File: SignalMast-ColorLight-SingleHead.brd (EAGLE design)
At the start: 13 x 39.8 mm, 4 parts

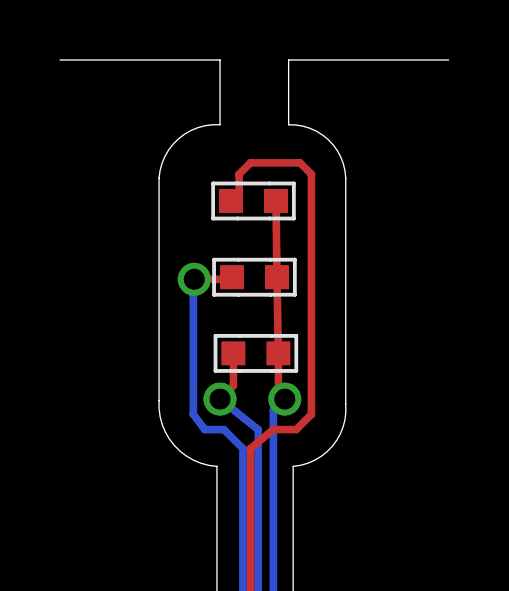
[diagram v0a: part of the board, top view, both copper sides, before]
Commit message: normalized values
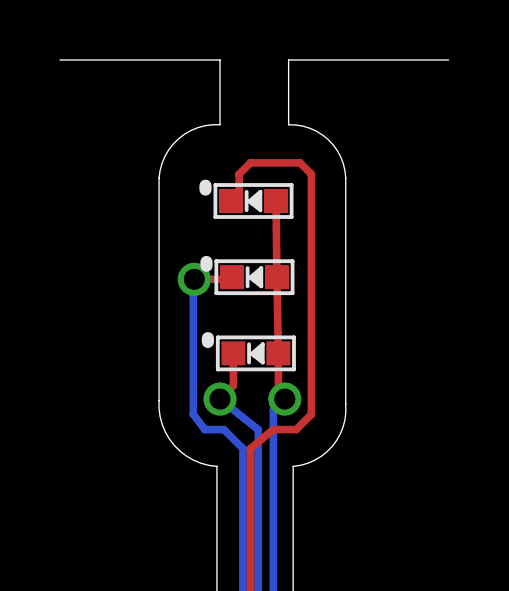
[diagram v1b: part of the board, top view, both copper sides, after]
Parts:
- GYR+: value CONNECTOR-GROVE-4P-2.0-3470130P1 -> 0.100
- turned LED1 to 0 degrees
- turned LED2 to 0 degrees
- turned LED3 to 0 degrees
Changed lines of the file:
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@@
 </autorouter>
 <elements>
-<element name="GYR+" library="SPCoast" package="1X04_LOCK" value="CONNECTOR-GROVE-4P-2.0-3470130P1" x="10.16" y="5.08" smashed="yes" rot="R180">
+<element name="GYR+" library="SPCoast" package="1X04_LOCK" value="0.100" x="10.16" y="5.08" smashed="yes" rot="R180">
 <attribute name="NAME" x="2.921" y="0.762" size="1.778" layer="25" font="vector" ratio="11" rot="SR0"/>
 </element>
-<element name="LED1" library="SPCoast" package="0603-LED" value="R" x="6.53" y="38.099" smashed="yes" rot="R180">
-<attribute name="OPL" value="19-217-R6C-AL1M2VY-3T" x="6.53" y="38.099" size="1.778" layer="27" rot="R180" display="off"/>
-<attribute name="VALUE" x="11.61" y="38.734" size="1.27" layer="27" rot="R180"/>
+<element name="LED1" library="SPCoast" package="0603-LED" value="R" x="6.53" y="38.099" smashed="yes">
+<attribute name="OPL" value="19-217-R6C-AL1M2VY-3T" x="6.53" y="38.099" size="1.778" layer="27" display="off"/>
+<attribute name="VALUE" x="1.45" y="37.464" size="1.27" layer="27"/>
 </element>
-<element name="LED2" library="SPCoast" package="0603-LED" value="Y" x="6.482" y="40.639" smashed="yes" rot="R180">
-<attribute name="OPL" value="19-217-Y5C-AM1N1VY-3T" x="6.482" y="40.639" size="1.778" layer="27" rot="R180" display="off"/>
-<attribute name="VALUE" x="11.562" y="41.274" size="1.27" layer="27" rot="R180"/>
+<element name="LED2" library="SPCoast" package="0603-LED" value="Y" x="6.482" y="40.639" smashed="yes">
+<attribute name="OPL" value="19-217-Y5C-AM1N1VY-3T" x="6.482" y="40.639" size="1.778" layer="27" display="off"/>
+<attribute name="VALUE" x="1.402" y="40.004" size="1.27" layer="27"/>
 </element>
-<element name="LED3" library="SPCoast" package="0603-LED" value="G" x="6.45" y="43.179" smashed="yes" rot="R180">
-<attribute name="OPL" value="19-217-G7C-AN1P2-3T " x="6.45" y="43.179" size="1.778" layer="27" rot="R180" display="off"/>
-<attribute name="VALUE" x="11.53" y="43.814" size="1.27" layer="27" rot="R180"/>
+<element name="LED3" library="SPCoast" package="0603-LED" value="G" x="6.45" y="43.179" smashed="yes">
+<attribute name="OPL" value="19-217-G7C-AN1P2-3T " x="6.45" y="43.179" size="1.778" layer="27" display="off"/>
+<attribute name="VALUE" x="1.37" y="42.544" size="1.27" layer="27"/>
 </element>
 </elements>

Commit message: Version 1.3
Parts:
- renumbered GYR+ to J
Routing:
- net BY: track 38.7 -> 37.7 mm
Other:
- board size 13 x 39.8 mm -> 12.8 x 48.3 mm
- board text added: "+"
- board text added: "G"
- board text added: "R"
- board text added: "Y"
- board text removed: "GYR+"
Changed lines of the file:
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@@
 <setting verticaltext="up"/>
 </settings>
-<grid distance="50" unitdist="mil" unit="mil" style="dots" multiple="2" display="yes" altdistance="25" altunitdist="mil" altunit="mil"/>
+<grid distance="50" unitdist="mil" unit="mil" style="dots" multiple="2" display="yes" altdistance="5" altunitdist="mil" altunit="mil"/>
 <layers>
 <layer number="1" name="Top" color="4" fill="1" visible="yes" active="yes"/>
@@
 <layer number="19" name="Unrouted" color="6" fill="1" visible="yes" active="yes"/>
 <layer number="20" name="Dimension" color="15" fill="1" visible="yes" active="yes"/>
-<layer number="21" name="tPlace" color="19" fill="1" visible="yes" active="yes"/>
+<layer number="21" name="tPlace" color="7" fill="1" visible="yes" active="yes"/>
 <layer number="22" name="bPlace" color="17" fill="1" visible="no" active="yes"/>
 <layer number="23" name="tOrigins" color="30" fill="1" visible="yes" active="yes"/>
@@
 <wire x1="7.7724" y1="34.332" x2="7.7724" y2="8.128" width="0" layer="20"/>
 <wire x1="0" y1="8.128" x2="5.2324" y2="8.128" width="0" layer="20"/>
-<text x="2.921" y="0.762" size="1.778" layer="1" font="vector" rot="SR0">GYR+</text>
+<text x="1.651" y="0.762" size="1.778" layer="21" font="vector" rot="SR0">G</text>
 <wire x1="3.302" y1="43.942" x2="5.334" y2="45.72" width="0" layer="20" curve="-90"/>
 <wire x1="9.525" y1="43.942" x2="7.62" y2="45.72" width="0" layer="20" curve="90"/>
-<rectangle x1="0" y1="-0.127" x2="12.827" y2="47.752" layer="52"/>
-<rectangle x1="-0.127" y1="0" x2="12.7" y2="34.29" layer="51"/>
-<wire x1="7.62" y1="47.879" x2="7.62" y2="45.72" width="0" layer="20"/>
-<wire x1="5.334" y1="45.72" x2="5.334" y2="47.879" width="0" layer="20"/>
-<wire x1="7.7724" y1="8.128" x2="12.8524" y2="8.128" width="0" layer="20"/>
-<wire x1="0" y1="47.879" x2="5.334" y2="47.879" width="0" layer="20"/>
-<wire x1="7.62" y1="47.879" x2="12.954" y2="47.879" width="0" layer="20"/>
-<rectangle x1="5.334" y1="45.72" x2="7.62" y2="47.879" layer="51"/>
+<rectangle x1="0" y1="-0.127" x2="12.827" y2="47.752" layer="22"/>
+<wire x1="7.62" y1="48.26" x2="7.62" y2="45.72" width="0" layer="20"/>
+<wire x1="5.334" y1="45.72" x2="5.334" y2="48.26" width="0" layer="20"/>
+<wire x1="7.7724" y1="8.128" x2="12.827" y2="8.128" width="0" layer="20"/>
+<wire x1="0" y1="48.26" x2="5.334" y2="48.26" width="0" layer="20"/>
+<wire x1="7.62" y1="48.26" x2="12.827" y2="48.26" width="0" layer="20"/>
+<rectangle x1="5.334" y1="45.72" x2="7.62" y2="48.26" layer="21"/>
+<text x="4.191" y="0.762" size="1.778" layer="21" font="vector" rot="SR0">Y</text>
+<text x="6.731" y="0.762" size="1.778" layer="21" font="vector" rot="SR0">R</text>
+<text x="9.271" y="0.762" size="2.1844" layer="21" font="vector" rot="SR0">+</text>
+<rectangle x1="5.2324" y1="8.128" x2="7.7724" y2="34.3408" layer="21"/>
+<rectangle x1="0" y1="3.556" x2="12.827" y2="8.128" layer="21"/>
+<wire x1="0" y1="48.26" x2="0" y2="0" width="0" layer="20"/>
+<wire x1="0" y1="0" x2="12.827" y2="0" width="0" layer="20"/>
+<wire x1="12.827" y1="0" x2="12.827" y2="8.128" width="0" layer="20"/>
+<wire x1="12.827" y1="8.128" x2="12.827" y2="48.26" width="0" layer="20"/>
 </plain>
 <attributes>
@@
 </autorouter>
 <elements>
-<element name="GYR+" library="SPCoast" package="1X04_LOCK" value="0.100" x="10.16" y="5.08" smashed="yes" rot="R180">
-<attribute name="NAME" x="2.921" y="0.762" size="1.778" layer="25" font="vector" ratio="11" rot="SR0"/>
+<element name="J" library="SPCoast" package="1X04_LOCK" value="0.100" x="10.16" y="5.08" smashed="yes" rot="R180">
+<attribute name="NAME" x="1.651" y="9.652" size="1.778" layer="25" font="vector" ratio="11" rot="SR0"/>
 </element>
 <element name="LED1" library="SPCoast" package="0603-LED" value="R" x="6.53" y="38.099" smashed="yes">
 <attribute name="OPL" value="19-217-R6C-AL1M2VY-3T" x="6.53" y="38.099" size="1.778" layer="27" display="off"/>
-<attribute name="VALUE" x="1.45" y="37.464" size="1.27" layer="27"/>
+<attribute name="VALUE" x="1.45" y="37.464" size="1.27" layer="21"/>
 </element>
 <element name="LED2" library="SPCoast" package="0603-LED" value="Y" x="6.482" y="40.639" smashed="yes">
 <attribute name="OPL" value="19-217-Y5C-AM1N1VY-3T" x="6.482" y="40.639" size="1.778" layer="27" display="off"/>
-<attribute name="VALUE" x="1.402" y="40.004" size="1.27" layer="27"/>
+<attribute name="VALUE" x="1.402" y="40.004" size="1.27" layer="21"/>
 </element>
 <element name="LED3" library="SPCoast" package="0603-LED" value="G" x="6.45" y="43.179" smashed="yes">
 <attribute name="OPL" value="19-217-G7C-AN1P2-3T " x="6.45" y="43.179" size="1.778" layer="27" display="off"/>
-<attribute name="VALUE" x="1.37" y="42.544" size="1.27" layer="27"/>
+<attribute name="VALUE" x="1.37" y="42.544" size="1.27" layer="21"/>
 </element>
 </elements>
 <signals>
 <signal name="BV+">
-<contactref element="GYR+" pad="1"/>
+<contactref element="J" pad="1"/>
 <contactref element="LED1" pad="A"/>
 <contactref element="LED2" pad="A"/>
@@
 <wire x1="7.62" y1="6.858" x2="7.112" y2="7.366" width="0.254" layer="16"/>
 <wire x1="7.112" y1="7.366" x2="7.112" y2="36.195" width="0.254" layer="16"/>
-<wire x1="7.112" y1="36.195" x2="7.493" y2="36.576" width="0.254" layer="16"/>
-<via x="7.493" y="36.576" extent="1-16" drill="0.7"/>
+<wire x1="7.112" y1="36.195" x2="7.366" y2="36.576" width="0.254" layer="16"/>
+<via x="7.366" y="36.576" extent="1-16" drill="0.6"/>
 <wire x1="7.493" y1="37.907" x2="7.28" y2="38.099" width="0.254" layer="1"/>
 <wire x1="7.2" y1="43.179" x2="7.232" y2="40.639" width="0.254" layer="1"/>
 <wire x1="7.232" y1="40.639" x2="7.28" y2="38.099" width="0.254" layer="1"/>
-<wire x1="7.493" y1="36.576" x2="7.28" y2="36.789" width="0.254" layer="1"/>
+<wire x1="7.366" y1="36.576" x2="7.28" y2="36.789" width="0.254" layer="1"/>
 <wire x1="7.28" y1="36.789" x2="7.28" y2="38.099" width="0.254" layer="1"/>
 </signal>
 <signal name="BR">
 <contactref element="LED1" pad="C"/>
-<contactref element="GYR+" pad="2"/>
+<contactref element="J" pad="2"/>
 <wire x1="7.62" y1="5.207" x2="7.112" y2="5.064" width="0.254" layer="16"/>
 <wire x1="7.112" y1="5.064" x2="7.112" y2="5.842" width="0.254" layer="16"/>
 <wire x1="7.112" y1="5.842" x2="6.604" y2="6.35" width="0.254" layer="16"/>
 <wire x1="6.604" y1="6.35" x2="6.604" y2="35.56" width="0.254" layer="16"/>
-<via x="5.334" y="36.576" extent="1-16" drill="0.7"/>
-<wire x1="6.604" y1="35.56" x2="5.334" y2="36.576" width="0.254" layer="16"/>
+<via x="5.588" y="36.576" extent="1-16" drill="0.6"/>
+<wire x1="6.604" y1="35.56" x2="5.588" y2="36.576" width="0.254" layer="16"/>
 <wire x1="5.78" y1="38.099" x2="5.78" y2="37.022" width="0.254" layer="1"/>
-<wire x1="5.78" y1="37.022" x2="5.334" y2="36.576" width="0.254" layer="1"/>
+<wire x1="5.78" y1="37.022" x2="5.588" y2="36.576" width="0.254" layer="1"/>
 </signal>
 <signal name="BY">
 <contactref element="LED2" pad="C"/>
-<contactref element="GYR+" pad="3"/>
+<contactref element="J" pad="3"/>
 <wire x1="5.08" y1="4.953" x2="6.096" y2="6.715" width="0.254" layer="16"/>
-<wire x1="6.096" y1="6.715" x2="6.096" y2="34.925" width="0.254" layer="16"/>
-<via x="4.476" y="40.57" extent="1-16" drill="0.7"/>
-<wire x1="4.476" y1="40.57" x2="5.98" y2="40.57" width="0.254" layer="1"/>
+<wire x1="6.096" y1="6.715" x2="6.096" y2="34.036" width="0.254" layer="16"/>
+<via x="4.73" y="39.3" extent="1-16" drill="0.6"/>
+<wire x1="4.73" y1="39.3" x2="5.98" y2="40.57" width="0.254" layer="1"/>
 <wire x1="5.98" y1="40.57" x2="5.732" y2="40.639" width="0.254" layer="1"/>
-<wire x1="6.096" y1="34.925" x2="5.461" y2="35.56" width="0.254" layer="16"/>
-<wire x1="5.461" y1="35.56" x2="4.826" y2="35.56" width="0.254" layer="16"/>
-<wire x1="4.826" y1="35.56" x2="4.445" y2="36.068" width="0.254" layer="16"/>
-<wire x1="4.445" y1="36.068" x2="4.445" y2="40.005" width="0.254" layer="16"/>
-<wire x1="4.445" y1="40.005" x2="4.476" y2="40.57" width="0.254" layer="16"/>
+<wire x1="4.73" y1="39.3" x2="4.191" y2="38.761" width="0.254" layer="16"/>
+<wire x1="4.191" y1="38.761" x2="4.191" y2="35.941" width="0.254" layer="16"/>
+<wire x1="4.191" y1="35.941" x2="6.096" y2="34.036" width="0.254" layer="16"/>
 </signal>
 <signal name="BG">
 <contactref element="LED3" pad="C"/>
-<contactref element="GYR+" pad="4"/>
+<contactref element="J" pad="4"/>
 <wire x1="2.54" y1="5.207" x2="4.239" y2="6.985" width="0.254" layer="1"/>
 <wire x1="4.239" y1="6.985" x2="5.715" y2="6.985" width="0.254" layer="1"/>
 <wire x1="5.715" y1="6.985" x2="6.35" y2="7.572" width="0.254" layer="1"/>
-<wire x1="6.35" y1="7.572" x2="6.35" y2="34.925" width="0.254" layer="1"/>
-<wire x1="6.35" y1="34.925" x2="7.112" y2="35.56" width="0.254" layer="1"/>
-<wire x1="7.112" y1="35.56" x2="7.874" y2="35.56" width="0.254" layer="1"/>
-<wire x1="7.874" y1="35.56" x2="8.382" y2="36.068" width="0.254" layer="1"/>
-<wire x1="8.382" y1="36.068" x2="8.382" y2="44.069" width="0.254" layer="1"/>
+<wire x1="6.35" y1="7.572" x2="6.35" y2="33.925" width="0.254" layer="1"/>
+<wire x1="8.382" y1="35.957" x2="8.382" y2="44.069" width="0.254" layer="1"/>
 <wire x1="8.382" y1="44.069" x2="8.001" y2="44.45" width="0.254" layer="1"/>
 <wire x1="8.001" y1="44.45" x2="6.35" y2="44.45" width="0.254" layer="1"/>
@@
 <wire x1="5.969" y1="44.069" x2="5.969" y2="43.091" width="0.254" layer="1"/>
 <wire x1="5.969" y1="43.091" x2="5.7" y2="43.179" width="0.254" layer="1"/>
+<wire x1="8.382" y1="35.957" x2="6.35" y2="33.925" width="0.254" layer="1"/>
 </signal>
 </signals>
